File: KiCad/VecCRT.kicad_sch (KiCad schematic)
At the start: 105 parts, among them J1 RaspiGPIO40, J2 Conn_02x08_Top_Bottom, J3 Conn_01x04_Female, Q1 2N7000, Q10 BSS138, Q11 BSS138, Q12 2N7002, Q13 BSS138, Q14 BSS138, Q2 2N7000, Q3 BSS138, Q4 2N7000, Q5 BSS138, Q6 2N7000, Q7 2N7002, Q8 2N7000, Q9 2N7000, U1 MCP4822, U2 4066, U3 4066, U4 TL072, U5 TL072, U6 4011, U7 40106, U8 4011, U9 LP2950-3.3

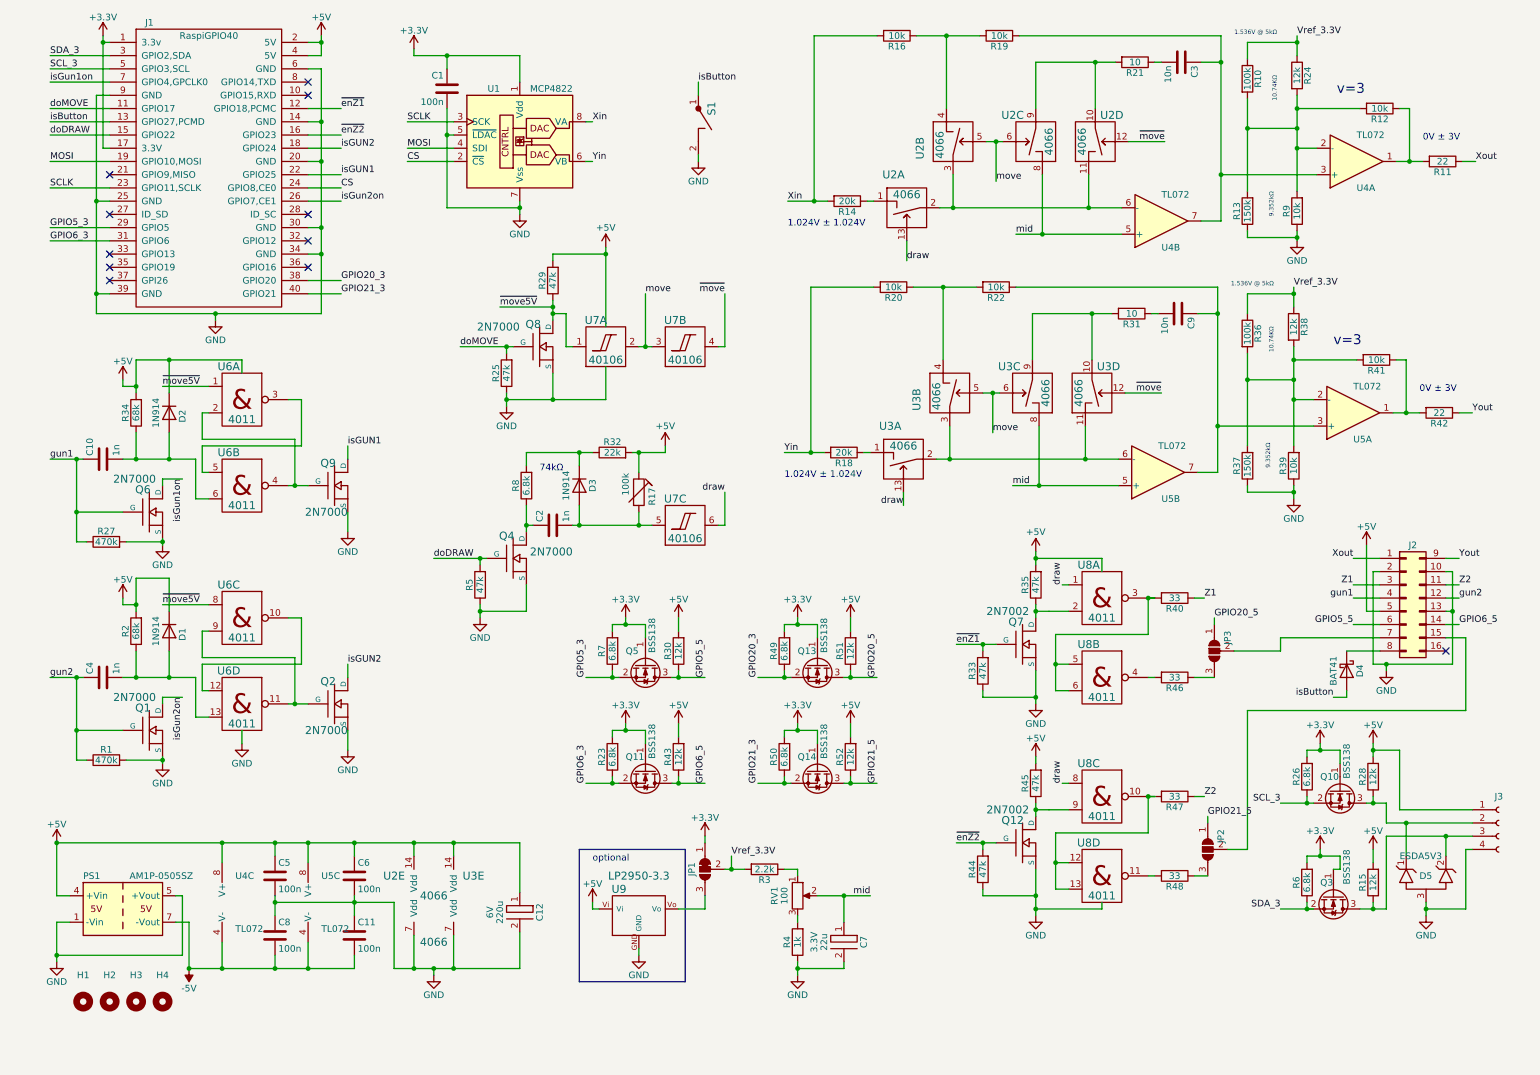
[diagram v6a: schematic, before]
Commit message: KiCad: EDA updates for PCB production; preliminary tap and switches; ReadMe.md updated
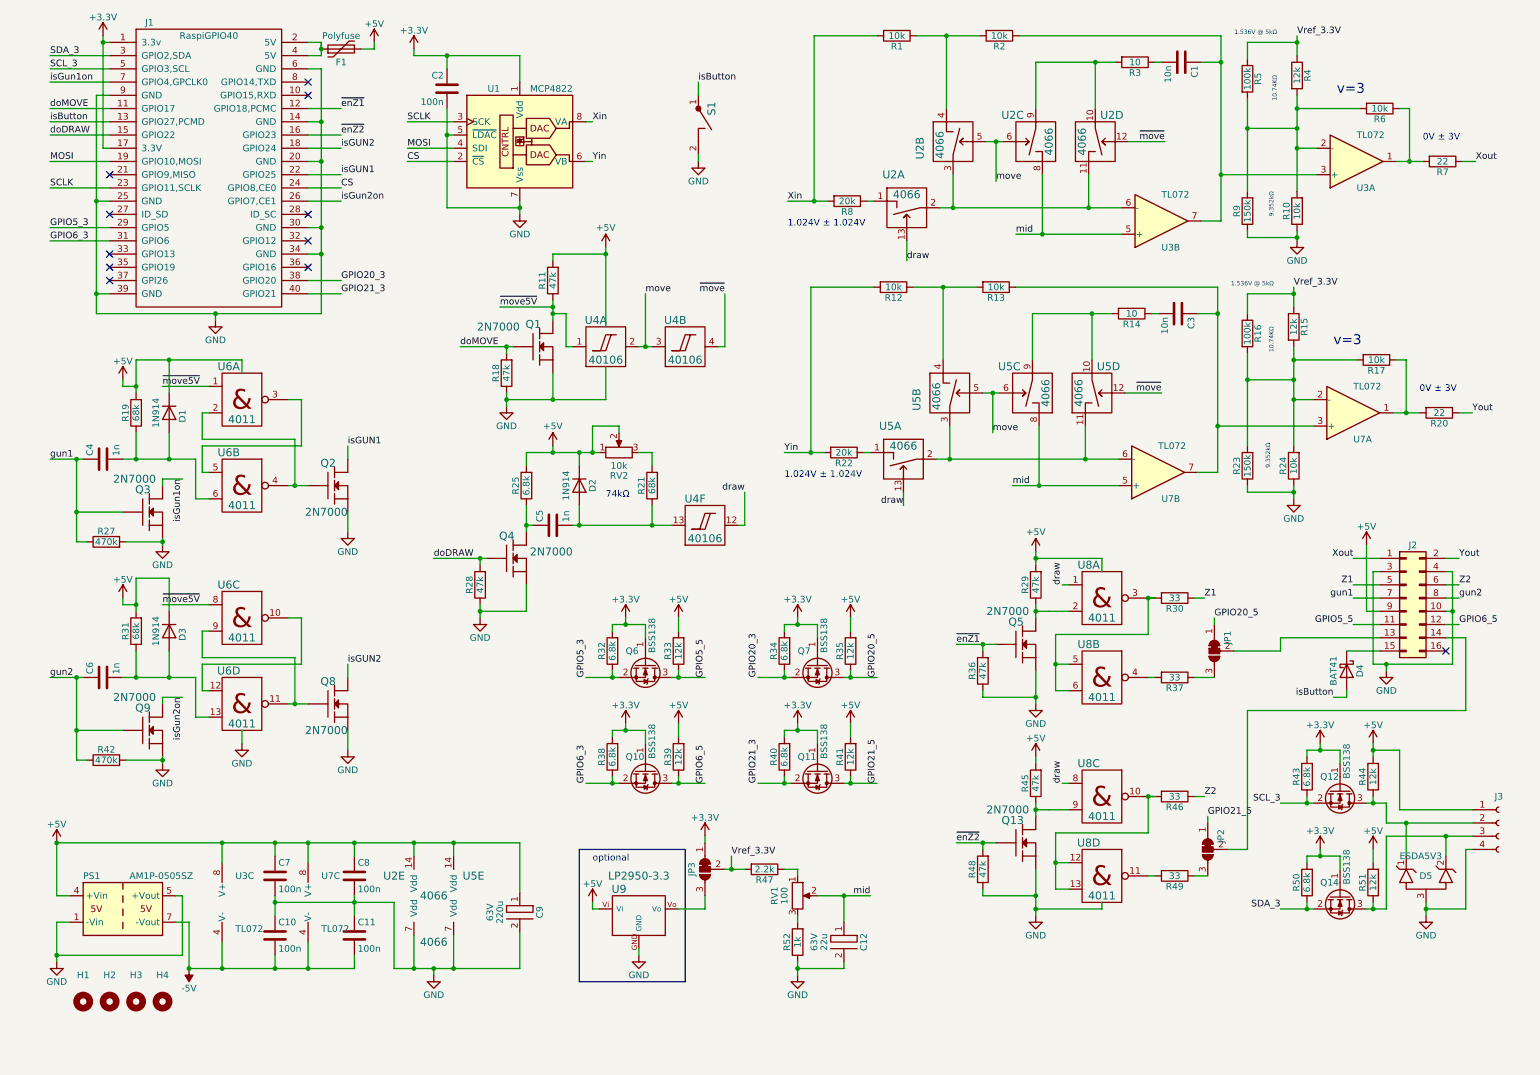
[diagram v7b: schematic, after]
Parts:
- removed J2: Conn_02x08_Top_Bottom, symbol Connector_Generic:Conn_02x08_Top_Bottom
- removed Q10, Q3: BSS138, Package_TO_SOT_SMD:SOT-23, symbol Transistor_FET:BSS138
- removed R17: 100k, symbol Device:R_Trim
- added F1: Polyfuse, Fuse:Fuse_Bourns_MF-RG300, symbol Device:Polyfuse
- added J2: Conn_02x08_Odd_Even, RG:Wannenstecker_2x08_V, symbol Connector_Generic:Conn_02x08_Odd_Even
- added Q12, Q14: BSS138, Package_TO_SOT_SMD:SOT-23, symbol Transistor_FET:BSS138
- added RV2: 10k, RG:Pot64y, symbol Device:R_Potentiometer
- C12: renamed from C7; Voltage 3.3V -> 63V
- C9: renamed from C12; Voltage 6V -> 63V
- J1: footprint Connector_PinHeader_2.54mm:PinHeader_2x20_P2.54mm_Vertical -> RG:Wannenstecker_2x20_V
- J3: footprint (none) -> RG:PSS_4
- JP1: renamed from JP3; footprint (none) -> Jumper:SolderJumper-3_P1.3mm_Bridged12_RoundedPad1.0x1.5mm; symbol Jumper:SolderJumper_3_Open -> Jumper:SolderJumper_3_Bridged12
- JP2: footprint (none) -> Jumper:SolderJumper-3_P1.3mm_Bridged12_RoundedPad1.0x1.5mm; symbol Jumper:SolderJumper_3_Open -> Jumper:SolderJumper_3_Bridged12
- JP3: renamed from JP1; footprint (none) -> Jumper:SolderJumper-3_P1.3mm_Bridged12_RoundedPad1.0x1.5mm
- Q13: renamed from Q12; value 2N7002 -> 2N7000; footprint RG:SOT-23_GDS -> RG:FETsgd_inline
- Q3: renamed from Q6; footprint RG:TO-92SGD -> RG:FETsgd_inline
- Q5: renamed from Q7; value 2N7002 -> 2N7000; footprint RG:SOT-23_GDS -> RG:FETsgd_inline
- Q9: renamed from Q1; footprint RG:TO-92SGD -> RG:FETsgd_inline
- R11: renamed from R29; footprint (none) -> RG:R4-2
- R18: renamed from R25; footprint (none) -> RG:SM-1206B
- R21: renamed from R32; value 22k -> 68k
- R28: renamed from R5; footprint RG:R4-2 -> RG:SM-1206B
- R29: renamed from R35; footprint RG:SM-1206B -> RG:R4-2
- R32: renamed from R7; footprint RG:R4-2 -> RG:SM-1206B
- R33: renamed from R30; footprint RG:R4-2 -> RG:SM-1206B
- R34: renamed from R49; footprint RG:R4-2 -> RG:SM-1206B
- R35: renamed from R51; footprint RG:R4-2 -> RG:SM-1206B
- R38: renamed from R23; footprint RG:R4-2 -> RG:SM-1206B
- R39: renamed from R43; footprint RG:R4-2 -> RG:SM-1206B
- R40: renamed from R50; footprint RG:R4-2 -> RG:SM-1206B
- R41: renamed from R52; footprint RG:R4-2 -> RG:SM-1206B
- R43: renamed from R26; footprint RG:R4-2 -> RG:SM-1206B
- R44: renamed from R28; footprint RG:R4-2 -> RG:SM-1206B
- R45: footprint RG:SM-1206B -> RG:R4-2
- R50: renamed from R6; footprint RG:R4-2 -> RG:SM-1206B
- R51: renamed from R15; footprint RG:R4-2 -> RG:SM-1206B
- RV1: footprint (none) -> RG:Pot64y
- U9: footprint (none) -> RG:TO-92ViGNDVo
- renumbered C3 to C1, C8 to C10, C1 to C2, C9 to C3, C10 to C4, C2 to C5, C4 to C6, C5 to C7, C6 to C8, D2 to D1, D3 to D2, D1 to D3, Q8 to Q1, Q11 to Q10, Q14 to Q11, Q9 to Q2, Q5 to Q6, Q13 to Q7, Q2 to Q8, R16 to R1, R9 to R10, R20 to R12, R22 to R13, R31 to R14, R38 to R15, R36 to R16, R41 to R17, R34 to R19, R19 to R2, R42 to R20, R18 to R22, R37 to R23, R39 to R24, R8 to R25, R21 to R3, R40 to R30, R2 to R31, R33 to R36, R46 to R37, R24 to R4, R1 to R42, R47 to R46, R3 to R47, R44 to R48, R48 to R49, R10 to R5, R4 to R52, R12 to R6, R11 to R7, R14 to R8, R13 to R9, U4 to U3, U7 to U4, U3 to U5, U5 to U7
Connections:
- net +3.3V: now also Q12.1 (G), Q14.1 (G)
- net +5V: now also D2.1 (K), R25.2, F1.2, J2.9 (Pin_9), RV2.1, RV2.2; no longer J1.2 (5V), J1.4 (5V), R21.2
- net GND: now also J2.10 (Pin_10), J2.3 (Pin_3), J2.4 (Pin_4)
- net GPIO5_5: now also J2.11 (Pin_11)
- net GPIO6_5: now also J2.12 (Pin_12)
- net SCL_3: now also Q12.2 (S)
- net SDA_3: now also Q14.2 (S)
- net Xout: now also J2.1 (Pin_1)
- net Yout: now also J2.2 (Pin_2)
- net Z1: now also J2.5 (Pin_5)
- net Z2: now also J2.6 (Pin_6)
- net draw: now also U4.12; no longer U4.6
- net gun1: now also J2.7 (Pin_7)
- net gun2: now also J2.8 (Pin_8)
- net at C5.2, D2.2 (A): now also R21.1, U4.13; no longer U4.5
- net at JP1.2 (C): now also J2.13 (Pin_13)
- net at D5.1 (K1), J3.2 (Pin_2), R44.1: now also Q12.3 (D)
- net at D5.2 (K2), J3.3 (Pin_3), R51.1: now also Q14.3 (D)
- net at JP2.2 (C): now also J2.14 (Pin_14)
- net at D4.1 (K): now also J2.15 (Pin_15)
- new net: R21.2, RV2.3
- new net: F1.1, J1.2 (5V), J1.4 (5V)
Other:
- moved on the sheet: R21, U4F

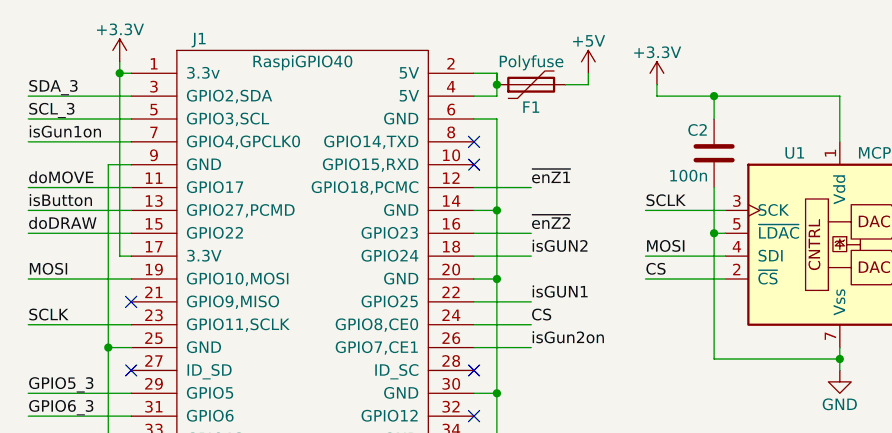
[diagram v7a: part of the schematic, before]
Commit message: Cut 3.3 / VccDAC for Arduino test
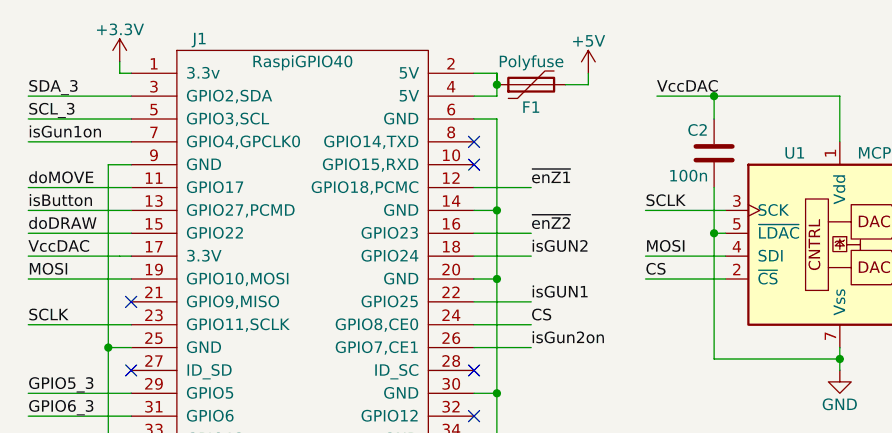
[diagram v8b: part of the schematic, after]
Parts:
- S1: footprint RG:Tast-DT6 -> RG:Tast2mil
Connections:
- net +3.3V: no longer C2.1, J1.17 (3.3V), U1.1 (Vdd)
- new net VccDAC: C2.1, J1.17 (3.3V), U1.1 (Vdd)
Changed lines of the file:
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@@
   (title_block
     (title "Vector Drawing for WWI")
-    (date "2023-08-29")
-    (rev "1.0c")
+    (date "2023-09-08")
+    (rev "1.0d")
   )
   (junction (at 62.23 26.67) (diameter 0) (color 0 0 0 0)
@@
   (junction (at 92.71 120.65) (diameter 0) (color 0 0 0 0)
   )
-  (junction (at 20.32 11.43) (diameter 0) (color 0 0 0 0)
-  )
   (junction (at 264.16 147.32) (diameter 0) (color 0 0 0 0)
   )
@@
     (stroke (width 0.3048) (type default) (color 0 0 0 0))
   )
+  (wire (pts (xy 10.16 31.75) (xy 20.32 31.75))
+    (stroke (width 0) (type default) (color 0 0 0 0))
+  )
   (wire (pts (xy 57.15 129.54) (xy 57.15 138.43))
     (stroke (width 0.3048) (type default) (color 0 0 0 0))
@@
     (stroke (width 0.3048) (type default) (color 0 0 0 0))
   )
-  (wire (pts (xy 80.01 12.7) (xy 80.01 13.97))
-    (stroke (width 0) (type default) (color 0 0 0 0))
-  )
   (wire (pts (xy 92.71 119.38) (xy 92.71 120.65))
     (stroke (width 0) (type default) (color 0 0 0 0))
@@
     (stroke (width 0) (type default) (color 0 0 0 0))
   )
-  (wire (pts (xy 20.32 31.75) (xy 20.32 11.43))
-    (stroke (width 0) (type default) (color 0 0 0 0))
-  )
   (wire (pts (xy 240.03 139.7) (xy 281.94 139.7))
     (stroke (width 0) (type default) (color 0 0 0 0))
@@
     (effects (font (size 1.27 1.27)) (justify left bottom))
   )
+  (label "VccDAC" (at 80.01 13.97 0)
+    (effects (font (size 1.27 1.27)) (justify left bottom))
+  )
   (label "CS" (at 66.04 39.37 0)
     (effects (font (size 1.27 1.27)) (justify left bottom))
@@
     (effects (font (size 1.27 1.27)) (justify left bottom))
   )
+  (label "VccDAC" (at 10.16 31.75 0)
+    (effects (font (size 1.27 1.27)) (justify left bottom))
+  )
   (label "GPIO21_3" (at 146.05 153.67 90)
     (effects (font (size 1.27 1.27)) (justify left bottom))
@@
       (effects (font (size 1.524 1.524)) hide)
     )
-    (property "Footprint" "RG:Tast-DT6" (id 2) (at 140.97 27.94 0)
+    (property "Footprint" "RG:Tast2mil" (id 2) (at 140.97 27.94 0)
       (effects (font (size 1.524 1.524)) hide)
     )
@@
     (pin "S")
   )
-  (symbol (lib_id "power:+3.3V") (at 80.01 12.7 0) (unit 1)
-    (in_bom yes) (on_board yes)
-    (property "Reference" "#PWR03" (id 0) (at 80.01 16.51 0)
-      (effects (font (size 1.27 1.27)) hide)
-    )
-    (property "Value" "+3.3V" (id 1) (at 80.01 9.144 0))
-    (property "Footprint" "" (id 2) (at 80.01 12.7 0)
-      (effects (font (size 1.27 1.27)) hide)
-    )
-    (property "Datasheet" "" (id 3) (at 80.01 12.7 0)
-      (effects (font (size 1.27 1.27)) hide)
-    )
-    (pin "1")
-  )
   (symbol (lib_id "Device:R") (at 97.79 74.93 180) (unit 1)
     (in_bom yes) (on_board yes)
@@
       (reference "#PWR02") (unit 1) (value "+5V") (footprint "")
     )
-    (path "/72818c6d-50e9-4f1e-a3c3-a08e9fbc7064"
-      (reference "#PWR03") (unit 1) (value "+3.3V") (footprint "")
-    )
     (path "/00000000-0000-0000-0000-0000645963e3"
       (reference "#PWR04") (unit 1) (value "GND") (footprint "")
@@
     )
     (path "/00000000-0000-0000-0000-000064595056"
-      (reference "S1") (unit 1) (value "TASTER") (footprint "RG:Tast-DT6")
+      (reference "S1") (unit 1) (value "TASTER") (footprint "RG:Tast2mil")
     )
     (path "/00000000-0000-0000-0000-000064769156"
